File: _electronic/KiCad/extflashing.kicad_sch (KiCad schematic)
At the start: 6 parts

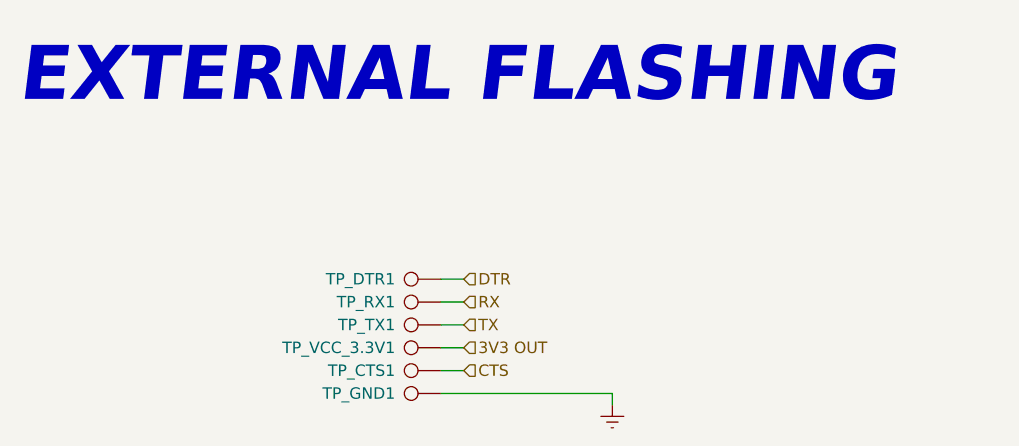
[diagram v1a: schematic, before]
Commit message: external flashing header
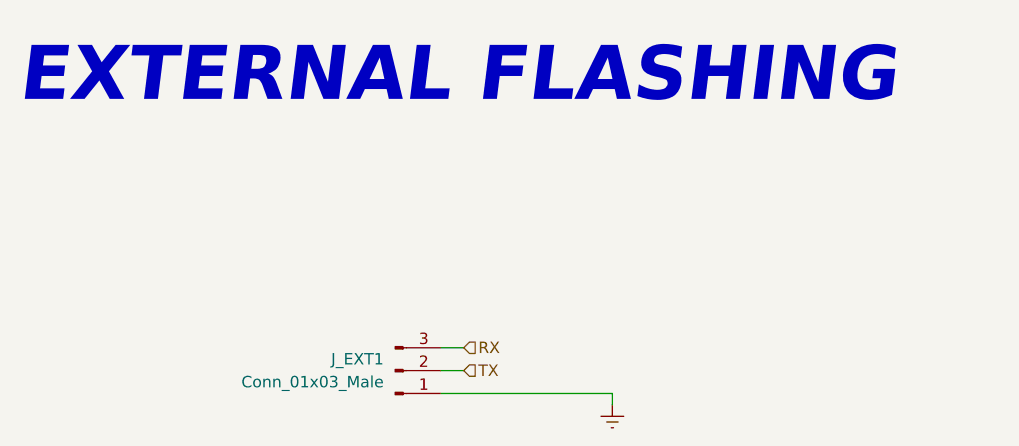
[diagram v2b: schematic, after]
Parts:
- removed TP_CTS1, TP_DTR1, TP_GND1, TP_RX1, TP_TX1, TP_VCC_3.3V1: TestPoint, TestPoint:TestPoint_Pad_D1.0mm, symbol Connector:TestPoint
- added J_EXT1: Conn_01x03_Male, Connector_PinHeader_2.54mm:PinHeader_1x03_P2.54mm_Horizontal, symbol Connector:Conn_01x03_Male
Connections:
- net GNDREF: now also J_EXT1.1 (Pin_1)
- net RX: now also J_EXT1.3 (Pin_3)
- net TX: now also J_EXT1.2 (Pin_2)
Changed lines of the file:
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@@
 (kicad_sch (version 20211123) (generator eeschema)
   (paper "A4")
-  (wire (pts (xy 140.97 107.95) (xy 143.51 107.95))
+  (wire (pts (xy 140.97 113.03) (xy 143.51 113.03))
     (stroke (width 0) (type default) (color 0 0 0 0))
   )
@@
     (stroke (width 0) (type default) (color 0 0 0 0))
   )
-  (wire (pts (xy 140.97 110.49) (xy 143.51 110.49))
-    (stroke (width 0) (type default) (color 0 0 0 0))
-  )
-  (wire (pts (xy 143.51 113.03) (xy 140.97 113.03))
-    (stroke (width 0) (type default) (color 0 0 0 0))
-  )
   (wire (pts (xy 140.97 115.57) (xy 160.02 115.57))
     (stroke (width 0) (type default) (color 0 0 0 0))
   )
-  (wire (pts (xy 143.51 102.87) (xy 140.97 102.87))
-    (stroke (width 0) (type default) (color 0 0 0 0))
-  )
-  (wire (pts (xy 140.97 105.41) (xy 143.51 105.41))
+  (wire (pts (xy 140.97 110.49) (xy 143.51 110.49))
     (stroke (width 0) (type default) (color 0 0 0 0))
   )
@@
     (effects (font (size 6 6) (thickness 0.6) bold italic) (justify left bottom))
   )
-  (hierarchical_label "3V3 OUT" (shape input) (at 143.51 110.49 0)
+  (hierarchical_label "RX" (shape input) (at 143.51 110.49 0)
     (effects (font (size 1.27 1.27)) (justify left))
   )
-  (hierarchical_label "DTR" (shape input) (at 143.51 102.87 0)
+  (hierarchical_label "TX" (shape input) (at 143.51 113.03 0)
     (effects (font (size 1.27 1.27)) (justify left))
   )
-  (hierarchical_label "RX" (shape input) (at 143.51 105.41 0)
-    (effects (font (size 1.27 1.27)) (justify left))
-  )
-  (hierarchical_label "CTS" (shape input) (at 143.51 113.03 0)
-    (effects (font (size 1.27 1.27)) (justify left))
-  )
-  (hierarchical_label "TX" (shape input) (at 143.51 107.95 0)
-    (effects (font (size 1.27 1.27)) (justify left))
-  )
-  (symbol (lib_id "Connector:TestPoint") (at 140.97 102.87 90) (unit 1)
-    (in_bom yes) (on_board yes)
-    (property "Reference" "TP_DTR1" (id 0) (at 135.89 102.87 90)
-      (effects (font (size 1.27 1.27)) (justify left))
+  (symbol (lib_id "Connector:Conn_01x03_Male") (at 135.89 113.03 0) (mirror x) (unit 1)
+    (in_bom yes) (on_board yes) (fields_autoplaced)
+    (property "Reference" "J_EXT1" (id 0) (at 134.62 111.7599 0)
+      (effects (font (size 1.27 1.27)) (justify right))
     )
-    (property "Value" "TestPoint" (id 1) (at 135.89 102.87 90)
-      (effects (font (size 1.27 1.27)) (justify left) hide)
+    (property "Value" "Conn_01x03_Male" (id 1) (at 134.62 114.2999 0)
+      (effects (font (size 1.27 1.27)) (justify right))
     )
-    (property "Footprint" "TestPoint:TestPoint_Pad_D1.0mm" (id 2) (at 140.97 97.79 0)
+    (property "Footprint" "Connector_PinHeader_2.54mm:PinHeader_1x03_P2.54mm_Horizontal" (id 2) (at 135.89 113.03 0)
       (effects (font (size 1.27 1.27)) hide)
     )
-    (property "Datasheet" "xxx" (id 3) (at 140.97 97.79 0)
-      (effects (font (size 1.27 1.27)) hide)
-    )
-    (property "#" "xxx" (id 5) (at 140.97 102.87 0)
-      (effects (font (size 1.27 1.27)) hide)
-    )
-    (property "Description" "Testing point" (id 6) (at 140.97 102.87 0)
-      (effects (font (size 1.27 1.27)) hide)
-    )
-    (property "Group" "External flash" (id 4) (at 140.97 102.87 0)
-      (effects (font (size 1.27 1.27)) hide)
-    )
-    (property "Mouser" "OK" (id 7) (at 140.97 102.87 0)
+    (property "Datasheet" "~" (id 3) (at 135.89 113.03 0)
       (effects (font (size 1.27 1.27)) hide)
     )
     (pin "1")
-  )
-  (symbol (lib_id "Connector:TestPoint") (at 140.97 107.95 90) (unit 1)
-    (in_bom yes) (on_board yes)
-    (property "Reference" "TP_TX1" (id 0) (at 135.89 107.95 90)
-      (effects (font (size 1.27 1.27)) (justify left))
-    )
-    (property "Value" "TestPoint" (id 1) (at 135.89 107.95 90)
-      (effects (font (size 1.27 1.27)) (justify left) hide)
-    )
-    (property "Footprint" "TestPoint:TestPoint_Pad_D1.0mm" (id 2) (at 140.97 102.87 0)
-      (effects (font (size 1.27 1.27)) hide)
-    )
-    (property "Datasheet" "xxx" (id 3) (at 140.97 102.87 0)
-      (effects (font (size 1.27 1.27)) hide)
-    )
-    (property "#" "xxx" (id 5) (at 140.97 107.95 0)
-      (effects (font (size 1.27 1.27)) hide)
-    )
-    (property "Description" "Testing point" (id 6) (at 140.97 107.95 0)
-      (effects (font (size 1.27 1.27)) hide)
-    )
-    (property "Group" "External flash" (id 4) (at 140.97 107.95 0)
-      (effects (font (size 1.27 1.27)) hide)
-    )
-    (property "Mouser" "OK" (id 7) (at 140.97 107.95 0)
-      (effects (font (size 1.27 1.27)) hide)
-    )
-    (pin "1")
-  )
-  (symbol (lib_id "Connector:TestPoint") (at 140.97 115.57 90) (unit 1)
-    (in_bom yes) (on_board yes)
-    (property "Reference" "TP_GND1" (id 0) (at 135.89 115.57 90)
-      (effects (font (size 1.27 1.27)) (justify left))
-    )
-    (property "Value" "TestPoint" (id 1) (at 135.89 115.57 90)
-      (effects (font (size 1.27 1.27)) (justify left) hide)
-    )
-    (property "Footprint" "TestPoint:TestPoint_Pad_D1.0mm" (id 2) (at 140.97 110.49 0)
-      (effects (font (size 1.27 1.27)) hide)
-    )
-    (property "Datasheet" "xxx" (id 3) (at 140.97 110.49 0)
-      (effects (font (size 1.27 1.27)) hide)
-    )
-    (property "#" "xxx" (id 5) (at 140.97 115.57 0)
-      (effects (font (size 1.27 1.27)) hide)
-    )
-    (property "Description" "Testing point" (id 6) (at 140.97 115.57 0)
-      (effects (font (size 1.27 1.27)) hide)
-    )
-    (property "Group" "External flash" (id 4) (at 140.97 115.57 0)
-      (effects (font (size 1.27 1.27)) hide)
-    )
-    (property "Mouser" "OK" (id 7) (at 140.97 115.57 0)
-      (effects (font (size 1.27 1.27)) hide)
-    )
-    (pin "1")
-  )
-  (symbol (lib_id "Connector:TestPoint") (at 140.97 110.49 90) (unit 1)
-    (in_bom yes) (on_board yes)
-    (property "Reference" "TP_VCC_3.3V1" (id 0) (at 135.89 110.49 90)
-      (effects (font (size 1.27 1.27)) (justify left))
-    )
-    (property "Value" "TestPoint" (id 1) (at 135.89 110.49 90)
-      (effects (font (size 1.27 1.27)) (justify left) hide)
-    )
-    (property "Footprint" "TestPoint:TestPoint_Pad_D1.0mm" (id 2) (at 140.97 105.41 0)
-      (effects (font (size 1.27 1.27)) hide)
-    )
-    (property "Datasheet" "xxx" (id 3) (at 140.97 105.41 0)
-      (effects (font (size 1.27 1.27)) hide)
-    )
-    (property "#" "xxx" (id 5) (at 140.97 110.49 0)
-      (effects (font (size 1.27 1.27)) hide)
-    )
-    (property "Description" "Testing point" (id 6) (at 140.97 110.49 0)
-      (effects (font (size 1.27 1.27)) hide)
-    )
-    (property "Group" "External flash" (id 4) (at 140.97 110.49 0)
-      (effects (font (size 1.27 1.27)) hide)
-    )
-    (property "Mouser" "OK" (id 7) (at 140.97 110.49 0)
-      (effects (font (size 1.27 1.27)) hide)
-    )
-    (pin "1")
-  )
-  (symbol (lib_id "Connector:TestPoint") (at 140.97 105.41 90) (unit 1)
-    (in_bom yes) (on_board yes)
-    (property "Reference" "TP_RX1" (id 0) (at 135.89 105.41 90)
-      (effects (font (size 1.27 1.27)) (justify left))
-    )
-    (property "Value" "TestPoint" (id 1) (at 135.89 105.41 90)
-      (effects (font (size 1.27 1.27)) (justify left) hide)
-    )
-    (property "Footprint" "TestPoint:TestPoint_Pad_D1.0mm" (id 2) (at 140.97 100.33 0)
-      (effects (font (size 1.27 1.27)) hide)
-    )
-    (property "Datasheet" "xxx" (id 3) (at 140.97 100.33 0)
-      (effects (font (size 1.27 1.27)) hide)
-    )
-    (property "#" "xxx" (id 5) (at 140.97 105.41 0)
-      (effects (font (size 1.27 1.27)) hide)
-    )
-    (property "Description" "Testing point" (id 6) (at 140.97 105.41 0)
-      (effects (font (size 1.27 1.27)) hide)
-    )
-    (property "Group" "External flash" (id 4) (at 140.97 105.41 0)
-      (effects (font (size 1.27 1.27)) hide)
-    )
-    (property "Mouser" "OK" (id 7) (at 140.97 105.41 0)
-      (effects (font (size 1.27 1.27)) hide)
-    )
-    (pin "1")
+    (pin "2")
+    (pin "3")
   )
   (symbol (lib_id "power:GNDREF") (at 160.02 116.84 0) (unit 1)
@@
       (effects (font (size 1.27 1.27)) hide)
     )
-    (pin "1")
-  )
-  (symbol (lib_id "Connector:TestPoint") (at 140.97 113.03 90) (unit 1)
-    (in_bom yes) (on_board yes)
-    (property "Reference" "TP_CTS1" (id 0) (at 135.89 113.03 90)
-      (effects (font (size 1.27 1.27)) (justify left))
-    )
-    (property "Value" "TestPoint" (id 1) (at 135.89 113.03 90)
-      (effects (font (size 1.27 1.27)) (justify left) hide)
-    )
-    (property "Footprint" "TestPoint:TestPoint_Pad_D1.0mm" (id 2) (at 140.97 107.95 0)
-      (effects (font (size 1.27 1.27)) hide)
-    )
-    (property "Datasheet" "xxx" (id 3) (at 140.97 107.95 0)
-      (effects (font (size 1.27 1.27)) hide)
-    )
-    (property "#" "xxx" (id 5) (at 140.97 113.03 0)
-      (effects (font (size 1.27 1.27)) hide)
-    )
-    (property "Description" "Testing point" (id 6) (at 140.97 113.03 0)
-      (effects (font (size 1.27 1.27)) hide)
-    )
-    (property "Group" "External flash" (id 4) (at 140.97 113.03 0)
-      (effects (font (size 1.27 1.27)) hide)
-    )
-    (property "Mouser" "OK" (id 7) (at 140.97 113.03 0)
-      (effects (font (size 1.27 1.27)) hide)
-    )

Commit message: schematics footer and export
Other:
- company: (none) -> Andrei Speridiao
- title: (none) -> E-TKT
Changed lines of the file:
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@@
 (kicad_sch (version 20211123) (generator eeschema)
   (paper "A4")
+  (title_block
+    (title "E-TKT")
+    (date "2022-07-21")
+    (rev "3")
+    (company "Andrei Speridiao")
+  )
   (wire (pts (xy 140.97 113.03) (xy 143.51 113.03))
     (stroke (width 0) (type default) (color 0 0 0 0))
